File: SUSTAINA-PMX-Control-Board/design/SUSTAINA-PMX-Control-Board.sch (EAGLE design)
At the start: 8 parts, among them M1 USB-TO-QUAD-RS-485-CONV-MODUL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

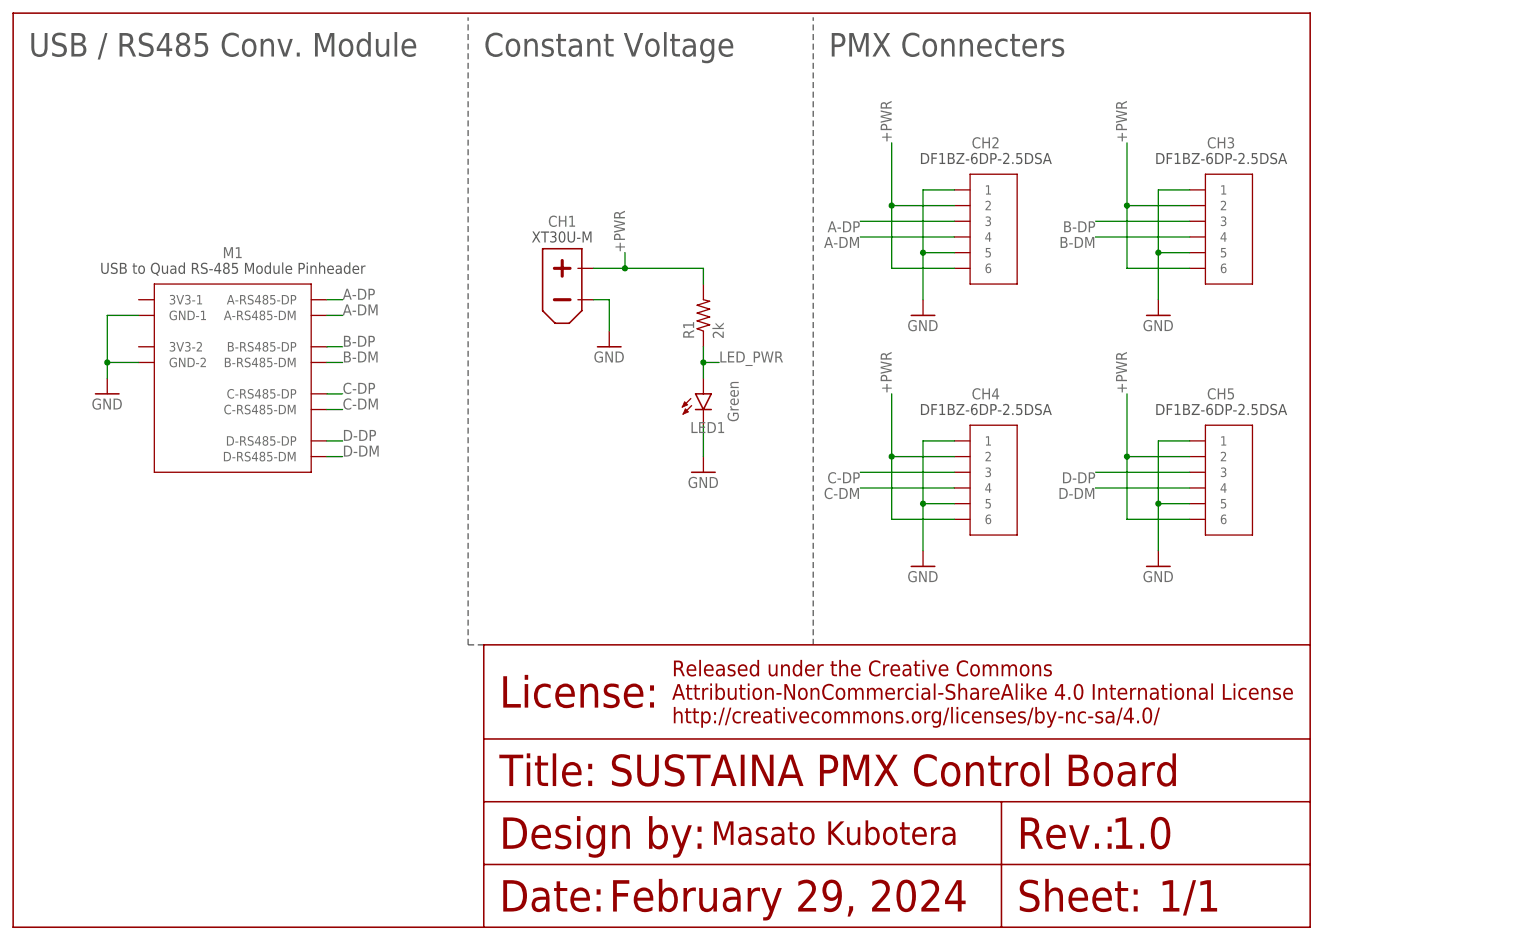
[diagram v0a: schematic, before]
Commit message: Add mass-produced version of PMX-Control-Board
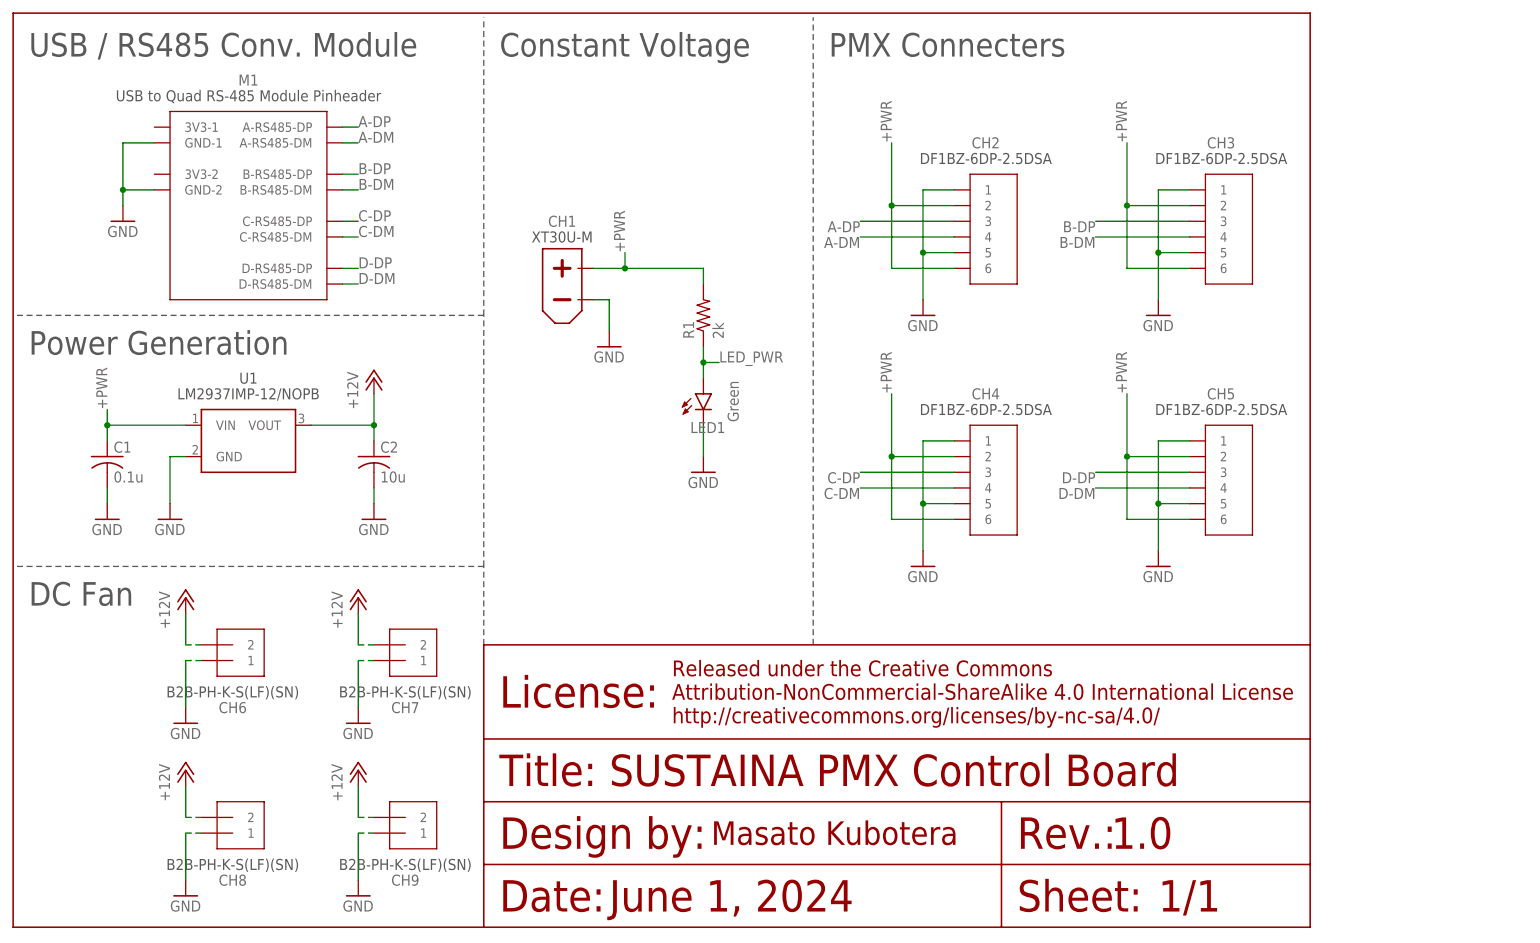
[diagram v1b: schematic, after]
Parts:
- added C1: 0.1u, rcl:C-USC0603
- added C2: 10u, rcl:C-USC0603
- added CH6, CH7, CH8, CH9: B2B-PH-K-S(LF)(SN), JST-PH:B2B-PH-K-S(LF)(SN)
- added U1: LM2937IMP-12NOPB, LM2937IMP-12NOPB:LM2937IMP-12NOPB
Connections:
- new net +12V: C2.1, CH6.2, CH7.2, CH8.2, CH9.2, U1.VOUT
- net +PWR: now also C1.1, U1.VIN
- net GND: now also C1.2, C2.2, CH6.1, CH7.1, CH8.1, CH9.1, U1.GND
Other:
- note added: "DC Fan"
- note added: "June 1, 2024"
- note added: "Power Generation"
- note removed: "February 29, 2024"
- moved on the sheet: M1
